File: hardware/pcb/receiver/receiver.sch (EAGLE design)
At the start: 68 parts, among them IC3 LM1117-5.0, IC4 TPS73733, X1 SMA

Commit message: hw: added pullup pulldown resistors to lvpecl
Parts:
- added R11, R12: 130R, rcl:R-EU_M1206
- added R13, R14: 83R, rcl:R-EU_M1206
- V1: value SY100EPT22 -> (none)
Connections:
- net N$19 renamed FILTERED_RF
- removed net N$20: IC5.ENC_P, V1.Q0
- removed net N$23: IC5.ENC_N, V1.!Q0
- new net ENC_N: IC5.ENC_N, R11.1, R14.2, V1.!Q0
- new net ENC_P: IC5.ENC_P, R12.1, R13.2, V1.Q0
- net +3V3: now also R11.2, R12.2
- net GND: now also R13.1, R14.1
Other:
- note added: "adc encode"
- moved on the sheet: C1, C10, C11, C12, C13, C14, C15, C16, C32, C33, C34, C8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

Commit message: hw: grouped power supply
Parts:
- added C38: 4,7u, rcl:CPOL-EUC
- C2, C21, C22, C34: device rcl:C-EUC0805 -> rcl:CPOL-EU140CLH-0810
- C23, C24, C25, C26, C27, C28, C29, C3, C30, C31, C4, C5: value 0,1u -> 100n
- D1: value CDSOD232-T03C -> CDSOD232
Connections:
- net N$12 renamed AMPOUT_P
- net N$7 renamed AMPOUT_N
- net VCC renamed N$7
- removed net N$21: SV1.GPIO_011
- removed net N$22: SV1.GPIO_013
- removed net N$31: SV1.GPIO_015
- removed net N$32: SV1.GPIO_017
- net +3V3: now also C22.+, L7.2; no longer C22.1
- net +5V: now also C21.+, C38.+; no longer C21.1, L7.2
- net DA0: no longer SV1.GPIO_019
- net DA1: no longer SV1.GPIO_021
- net DA10: no longer SV1.GPIO_028
- net DA11: no longer SV1.GPIO_026
- net DA12: no longer SV1.GPIO_024
- net DA13: no longer SV1.GPIO_022
- net DA14: no longer SV1.GPIO_020
- net DA15: no longer SV1.GPIO_018
- net DA2: no longer SV1.GPIO_023
- net DA3: no longer SV1.GPIO_025
- net DA4: no longer SV1.GPIO_027
- net DA5: no longer SV1.GPIO_029
- net DA6: no longer SV1.GPIO_031
- net DA7: no longer SV1.GPIO_033
- net DA8: no longer SV1.GPIO_032
- net DA9: no longer SV1.GPIO_030
- net GND: now also C2.-, C21.-, C22.-, C34.+, C38.-; no longer C2.2, C21.2, C22.2, C34.1
- net N$53: now also C2.+; no longer C2.1
- net VCM: now also C34.-; no longer C34.2
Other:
- note added: "C33 - optional for RC/LC filter"
- note added: "adc digital and analog vcc fitlering"
- note removed: "adc analog vcc fitlering"
- note removed: "adc digital vcc fitlering"
- note removed: "optional cap for RC/LC filter"
- moved on the sheet: C1, C10, C11, C12, C13, C14, C15, C16, C18, C19, C20, C23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

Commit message: hw: added manufacturer code for elements
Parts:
- removed C32, C35: 100n, rcl:C-EUC0805
- removed C38: 4,7u, rcl:CPOL-EUC
- removed IC4: TPS73733, texas:TPS77001
- added C39: 10n, rcl:C-EUC0805
- added C40: 10u, rcl:C-EUC0805
- added IC1: REG1117, burr-brown:REG1117
- added LED1: (no value), led:LEDSML0805
- added R15: 2k, rcl:R-EU_M1206
- C1, C16, C17, C18, C23, C24, C25, C26, C27, C28, C29, C3, C30, C31, C36, C37, C4, C5, C8: MFR (none) -> C0805C104K5RACTU
- C19: device rcl:CPOL-EUC -> rcl:C-EUC0805; MFR (none) -> VJ0805G106KXQTW1BC
- C2: value 2,2u -> 100n; device rcl:CPOL-EU140CLH-0810 -> rcl:C-EUC0805; MFR (none) -> C0805C104K5RACTU
- C20: value 100u -> 4,7u; device rcl:CPOL-EUC -> rcl:C-EUC0805; MFR (none) -> 08056D475KAT2A
- C21: device rcl:CPOL-EU140CLH-0810 -> rcl:C-EUC0805; MFR (none) -> 08056D475KAT2A
- C22: value 4,7u -> 2,2u; device rcl:CPOL-EU140CLH-0810 -> rcl:C-EUC0805; MFR (none) -> VJ0805G225KXQTW1BC
- C34: device rcl:CPOL-EU140CLH-0810 -> rcl:C-EUC0805; MFR (none) -> VJ0805G225KXQTW1BC
- D1: MFR (none) -> CDSOD323-T03C
- F1: value 800mA -> (none); device fuse:GSH15 -> lstolcman_thesis:0ZCG0150BF2C; MFR (none) -> 0ZCG0150BF2C
- IC3: value LM1117-5.0 -> (none); device linear:7806DT -> lstolcman_thesis:TPS73733; MFR (none) -> 595-TPS73733DCQR
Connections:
- removed net N$52: C32.1, R10.2, X1.1
- new net N$12: LED1.C, R15.2
- new net N$19: C39.1, IC3.NR
- net +3V3: now also C16.2, C17.2, C2.2, C21.1, C28.2, C29.2, IC3.OUT; no longer C22.+, C3.2, C31.1, C35.1, C4.2, C5.2, IC4.OUT
- net +5V: now also C18.2, C19.1, C20.1, C30.2, IC1.VOUT, IC3.EN, IC3.IN, LED1.A; no longer C17.1, C20.+, C21.+, C36.1, C38.+, IC3.VO, IC4.!EN, IC4.IN
- net +5V_AMP: now also C8.2; no longer C37.2
- net FILTERED_RF: now also C36.1; no longer C16.1
- net GND: now also C16.1, C17.1, C18.1, C19.2, C2.1, C20.2, C21.2, C22.1, C31.1, C34.2, C39.2, C40.2, IC1.GND, IC3.GND1, IC3.GND2, R15.1; no longer C17.2, C18.2, C19.-, C2.-, C20.-, C21.-, C22.-, C31.2, C34.+, C35.2, C36.2, C38.-, IC3.GND, IC4.GND
- net N$15: now also C37.2; no longer C8.2
- net N$2: now also R10.2, X1.1; no longer C32.2
- net N$3: now also C36.2; no longer C16.2
- net N$53: now also C34.1; no longer C2.+
- net N$7: now also C31.2, C40.1, IC1.VIN; no longer C18.1, C19.+, IC3.VI
- net VCM: now also C22.2; no longer C34.-
- net VDD: now also C3.2, C4.2, C5.2; no longer C28.2, C29.2, C30.2
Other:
- note added: "enc is LVPECL!"
- note added: "use SY100EPT22 or mc100lvelt22"
- note removed: "enc is lvpecl!!!!"
- note removed: "or mc100lvelt22!"
- note removed: "ptc?"
- moved on the sheet: C1, C10, C11, C12, C13, C14, C15, C16, C17, C18, C23, C24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

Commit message: hw: added parts id to reciever
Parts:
- removed C34: 2,2u, rcl:C-EUC0805
- removed L9: ferrite bead, inductor-neosid:SM-NE29
- removed S1: (no value), switch:255SB
- added C32: 100n, rcl:C-EUC0805
- added D2: (no value), diode:DIODE-DO214AC
- C33: MFR (none) -> C0805C101J5GACTU
- C6, C7: MFR (none) -> VJ0805A2R7BXQPW1BC
- IC2, IC5: MFR (none) -> Linear
- J2: MFR (none) -> 163-179PH-EX
- JP1: device pinhead:PINHD-2X4 -> lstolcman_thesis:PINHD-2X4; MFR (none) -> 54202-S08-04
- L4, L5, L6, L7: MFR (none) -> 2508056007Y3
- LED1: MFR (none) -> 720-LGR971-KN-1; MOUSER 720-LGR971-KN-1 -> (none)
- R1, R2: device rcl:R-EU_M1206 -> rcl:R-EU_M0805; MFR (none) -> RC0805FR-0751RL
- R10: device rcl:R-EU_M1206 -> rcl:R-EU_M0805; MFR (none) -> RC0805FR-071ML
- R11, R12: device rcl:R-EU_M1206 -> rcl:R-EU_M0805; MFR (none) -> RC0805FR-07130RL
- R13, R14: value 83R -> 82R; device rcl:R-EU_M1206 -> rcl:R-EU_M0805; MFR (none) -> RC0805FR-0782RL
- R15: device rcl:R-EU_M1206 -> rcl:R-EU_M0805; MFR (none) -> RC0805FR-072K2L
- R3, R4, R5, R6: device rcl:R-EU_M1206 -> rcl:R-EU_M0805; MFR (none) -> RC0805FR-07100RL
- R7, R8, R9: device rcl:R-EU_M1206 -> rcl:R-EU_M0805; MFR (none) -> RC0805FR-0710KLRC0805FR-0710KL
- SV1: MFR (none) -> 929975-01-20
- V1: MFR (none) -> SY100EPT22VZG-TR
- renumbered L8 to L6
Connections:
- removed net N$53: C34.1, L4.1, L5.2
- removed net N$8: J2.3, S1.P
- new net N$20: D2.A, J2.3
- net +3V3: now also L4.1; no longer L9.1
- net +3V3A_ADC: now also C32.1
- net +5V: now also L5.2; no longer L4.2
- net GND: now also C32.2; no longer C34.2
- net N$13: now also D2.C; no longer S1.O
- net VDD: now also L4.2; no longer L9.2
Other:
- note added: "http://cz.mouser.com/Passive-Components/Transformers-Audio-Signal/_/N-5gbg?Keyword=balun&Ns=Pricing|0"
- moved on the sheet: F1, J2, L4, L5, L7

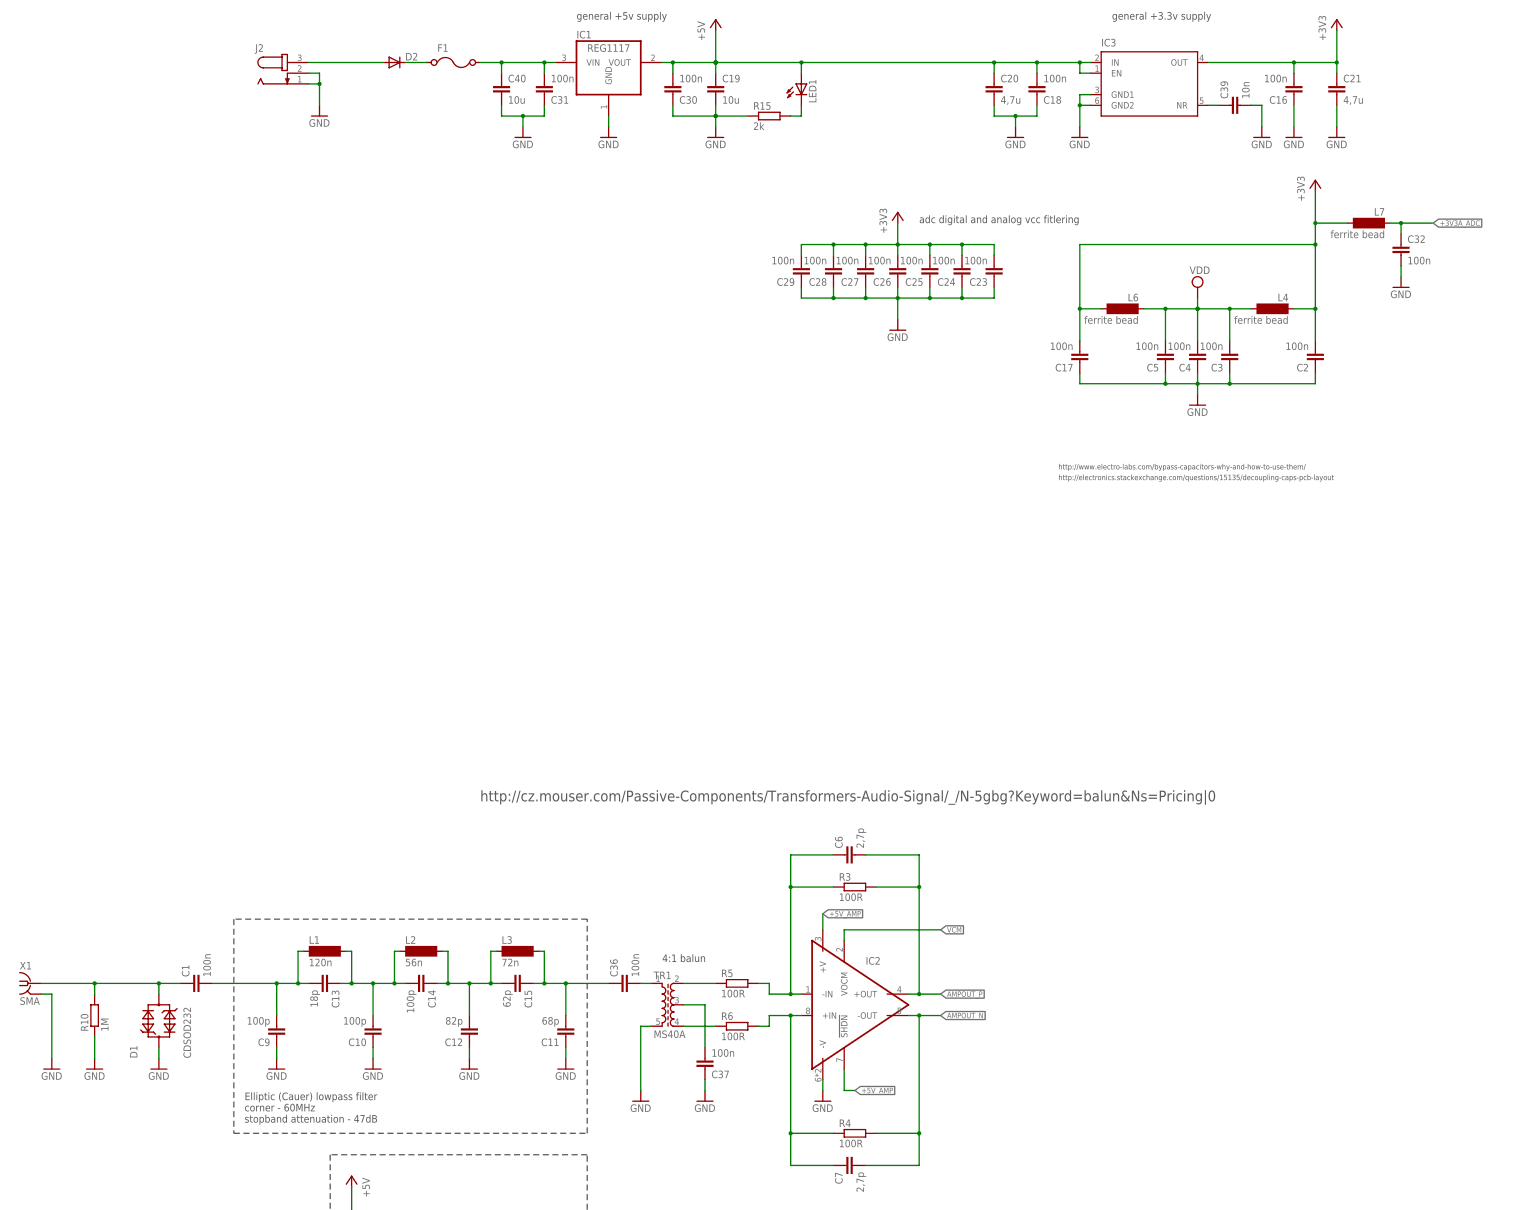
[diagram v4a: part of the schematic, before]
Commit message: hw: added bibliography, fitler for 55MHz cutoff
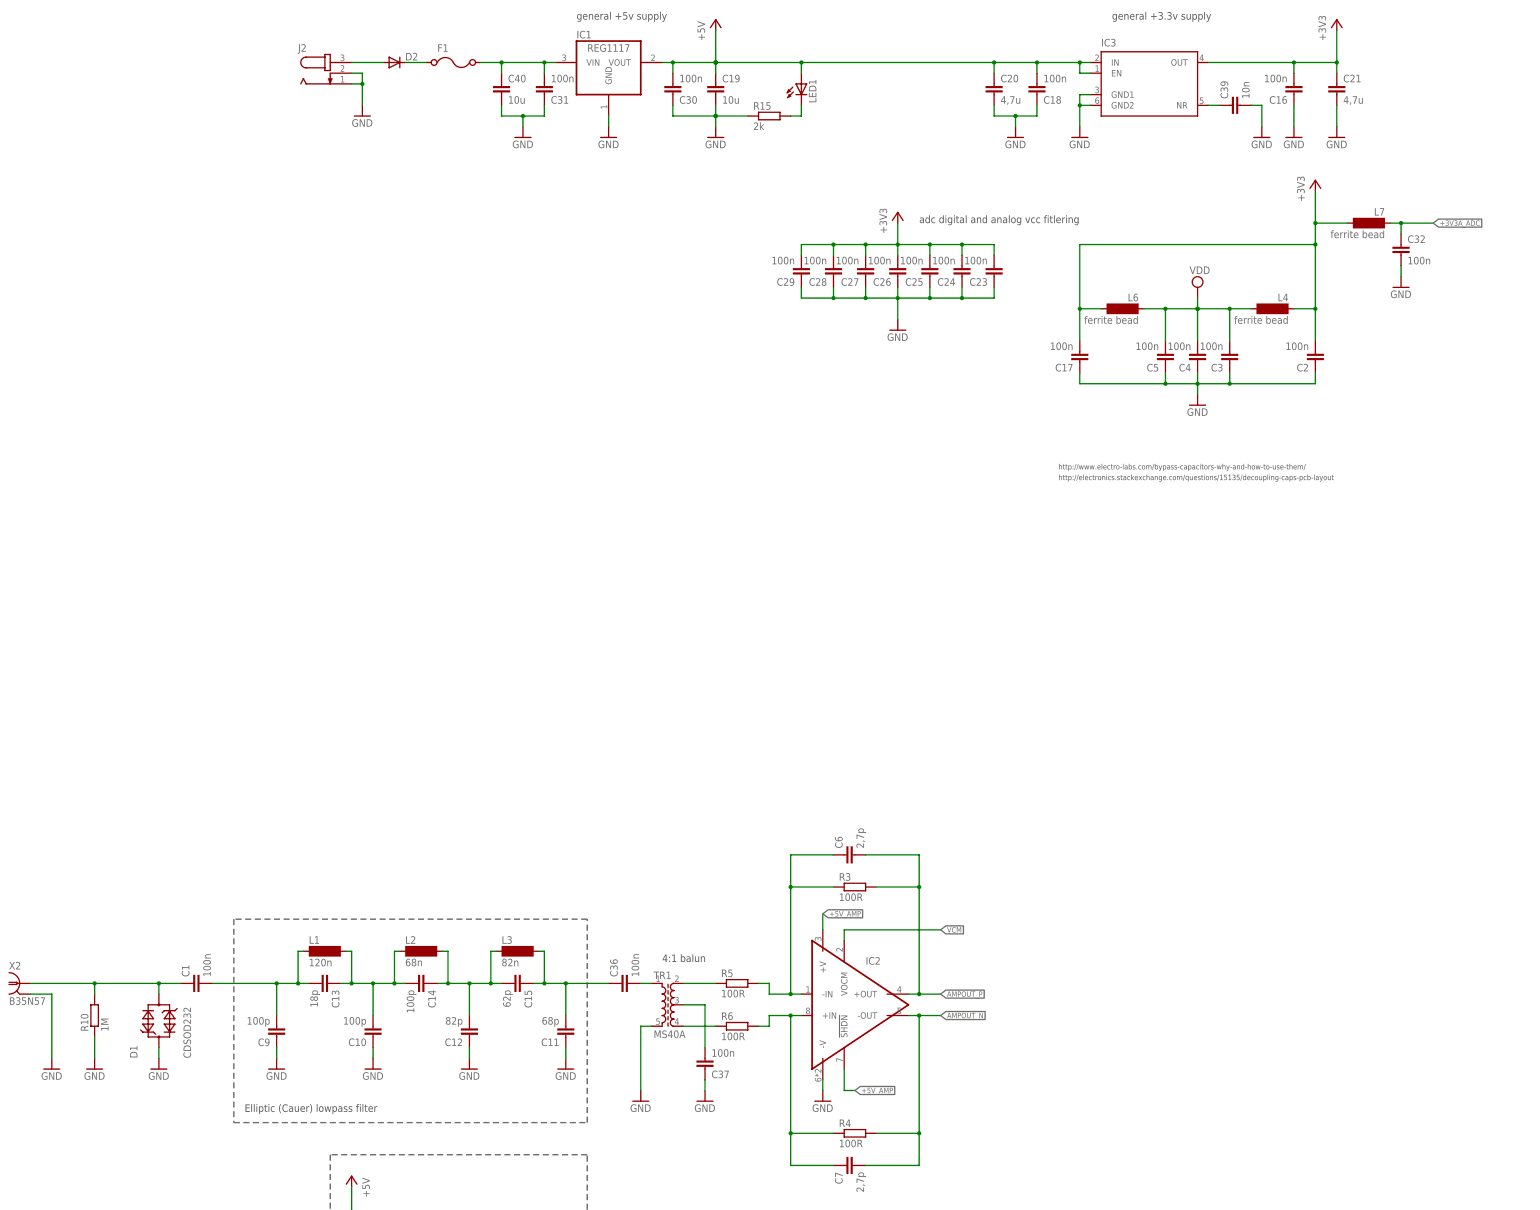
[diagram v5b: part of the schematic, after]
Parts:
- removed X1: SMA, con-coax:SMA-142-0701-801/806
- added X2: B35N57, con-coax:B35N57
- C10, C14, C9: MFR (none) -> C0805C101J5GACTU
- C11: MFR (none) -> C0805C680J5GACTU
- C12: MFR (none) -> 08055A820JAT2A
- C13: MFR (none) -> C0805C180J5GACTU
- C15: MFR (none) -> 08051A620JAT2A
- IC1: MFR 863-NCP1117ST50T3G -> NCV1117ST50T3G
- IC2: MFR Linear -> LTC6405IMS8E
- IC5: MFR Linear -> LTC2208CUP
- L1: MFR (none) -> CE201210-R12J
- L2: value 56n -> 68n; MFR (none) -> CE201210-68NJ
- L3: value 72n -> 82n; MFR (none) -> CE201210-82NJ
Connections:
- net GND: now also X2.2; no longer X1.2
- net N$2: now also X2.1; no longer X1.1
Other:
- note added: "Elliptic (Cauer) lowpass filter"
- note removed: "Elliptic (Cauer) lowpass filter corner - 60MHz stopband attenuation - 47dB"
- note removed: "http://cz.mouser.com/Passive-Components/Transformers-Audio-Signal/_/N-5gbg?Keyword=balun&Ns=Pricing|0"
- moved on the sheet: J2
